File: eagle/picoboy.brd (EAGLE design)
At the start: 72 x 121.7 mm, 14 parts

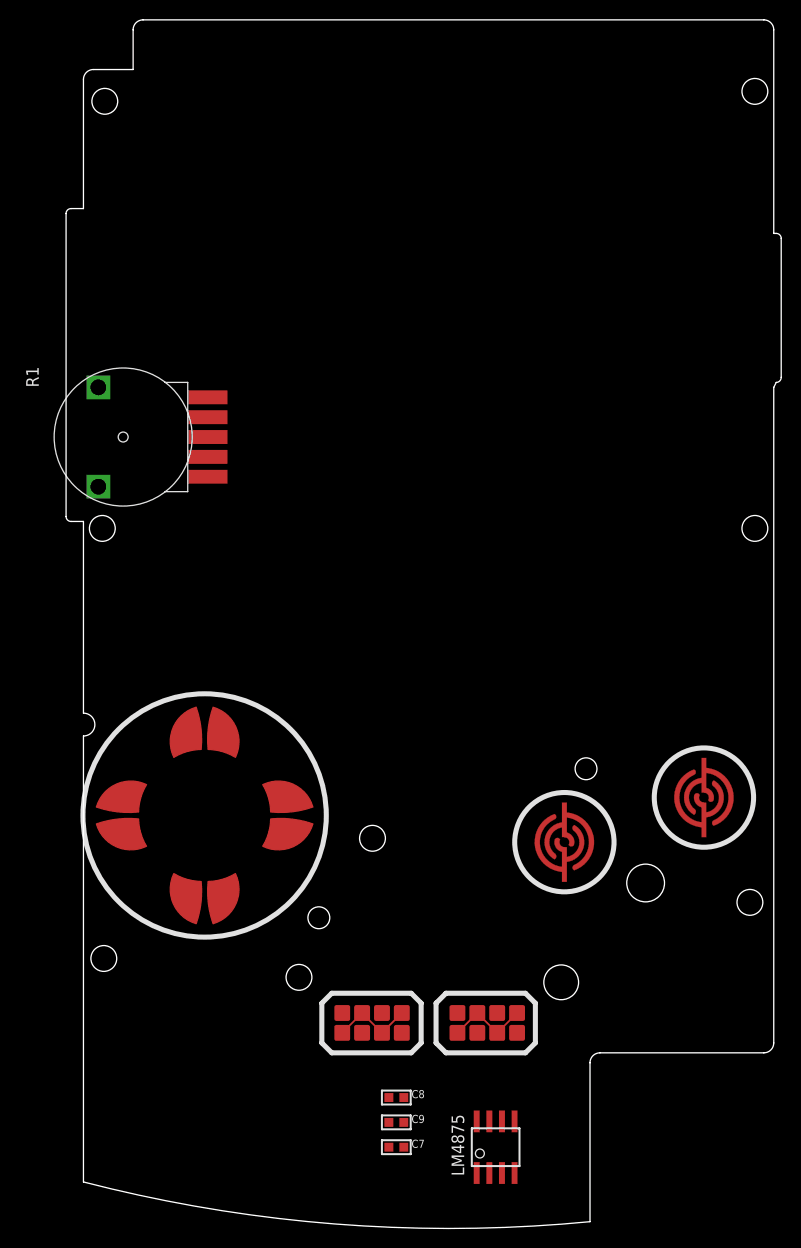
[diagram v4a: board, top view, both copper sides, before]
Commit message: Wired all audio components
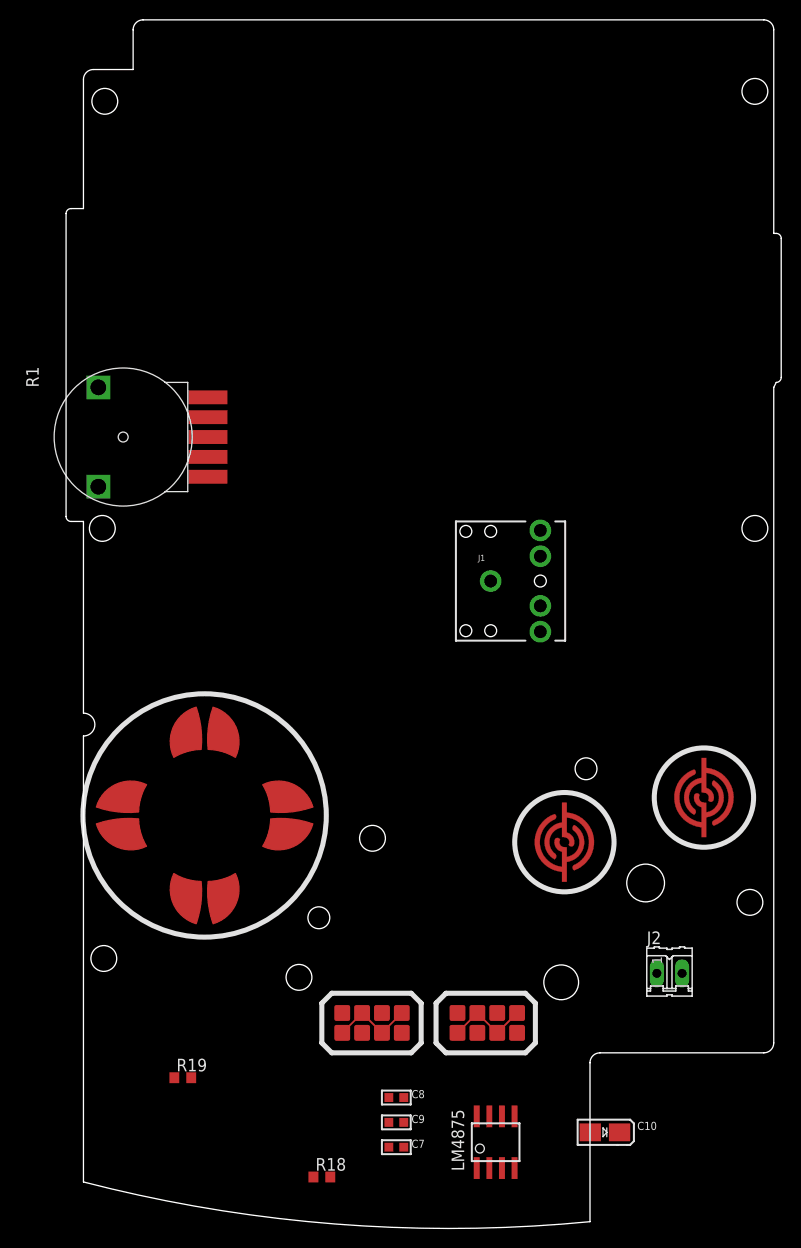
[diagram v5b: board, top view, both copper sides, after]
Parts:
- added C10: 100uF, picoboy:PICOBOY_CAPACITOR_EIA3216-18/A-W
- added J1: PICOBOY_AUDIO_JACK_3.5MM_KIT, picoboy:PICOBOY_AUDIO-JACK-KIT
- added J2: SPKR, con-amp-quick:02P
- added R18: 150 Ohms, rcl:R0603
- added R19: 100K, rcl:R0603
- moved LM4875 0.50 mm to (41.5, 4.00)
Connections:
- net N$1 renamed BYP
- net N$3 renamed VIN
- net N$4 renamed DC_VOL
- removed net N$2: C9.1, LM4875.1
- new net HPSENSE: J1.RSH, J1.TSH, LM4875.3, R19.1
- new net N$7: C10.-, J1.RING, J1.TIP, R18.2
- new net VOUT1: C10.+, J2.1, LM4875.5
- new net VOUT2: J2.2, LM4875.8
- net 3V3: now also C9.1, LM4875.1, R19.2
- net GND: now also J1.SLEEVE, R18.1
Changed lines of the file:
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@@
 <setting verticaltext="up"/>
 </settings>
-<grid distance="0.5" unitdist="mm" unit="mm" style="lines" multiple="1" display="yes" altdistance="0.125" altunitdist="mm" altunit="mm"/>
+<grid distance="0.5" unitdist="mm" unit="mm" style="lines" multiple="1" display="no" altdistance="0.125" altunitdist="mm" altunit="mm"/>
 <layers>
 <layer number="1" name="Top" color="4" fill="1" visible="yes" active="yes"/>
@@
 <element name="SELECT" library="picoboy" package="PICOBOY_CONDUCTIVE_BUTTON_THICK_STARTSELECT" value="PICOBOY_CONDUCTIVE_BUTTON_STARTSELECTCONDUCTIVE_BUTTON_THICK_STARTSELECT" x="29.055" y="16.01" smashed="yes"/>
 <element name="START" library="picoboy" package="PICOBOY_CONDUCTIVE_BUTTON_THICK_STARTSELECT" value="PICOBOY_CONDUCTIVE_BUTTON_STARTSELECTCONDUCTIVE_BUTTON_THICK_STARTSELECT" x="40.655" y="16.01" smashed="yes"/>
-<element name="LM4875" library="picoboy" package="PICOBOY_LM4875" value="PICOBOY_LM4875" x="41.5" y="3.5" smashed="yes">
-<attribute name="NAME" x="38.333" y="0.595" size="1.27" layer="25" rot="R90"/>
+<element name="LM4875" library="picoboy" package="PICOBOY_LM4875" value="PICOBOY_LM4875" x="41.5" y="4" smashed="yes">
+<attribute name="NAME" x="38.333" y="1.095" size="1.27" layer="25" rot="R90"/>
 </element>
 <element name="U$1" library="picoboy" package="PICOBOY_GBC_BOARD_OUTLINE" value="" x="0" y="0" smashed="yes"/>
@@
 <attribute name="NAME" x="-4.5" y="80" size="1.27" layer="25" rot="R90"/>
 <attribute name="VALUE" x="-2.5" y="80" size="1.27" layer="27" rot="R90"/>
+</element>
+<element name="J2" library="con-amp-quick" library_urn="urn:adsk.eagle:library:125" package="02P" package3d_urn="urn:adsk.eagle:package:5956/1" value="SPKR" x="59" y="21" smashed="yes">
+<attribute name="MF" value="" x="59" y="21" size="1.778" layer="27" display="off"/>
+<attribute name="MPN" value="" x="59" y="21" size="1.778" layer="27" display="off"/>
+<attribute name="NAME" x="56.714" y="23.9464" size="1.27" layer="25" ratio="10"/>
+<attribute name="OC_FARNELL" value="unknown" x="59" y="21" size="1.778" layer="27" display="off"/>
+<attribute name="OC_NEWARK" value="unknown" x="59" y="21" size="1.778" layer="27" display="off"/>
+<attribute name="POPULARITY" value="33" x="59" y="21" size="1.778" layer="27" display="off"/>
+<attribute name="VALUE" x="56.714" y="17.1646" size="1.27" layer="27" ratio="10"/>
+</element>
+<element name="J1" library="picoboy" package="PICOBOY_AUDIO-JACK-KIT" value="PICOBOY_AUDIO_JACK_3.5MM_KIT" x="41" y="60.5" smashed="yes">
+<attribute name="NAME" x="39.73" y="62.532" size="0.6096" layer="25" font="vector" ratio="20"/>
+<attribute name="PROD_ID" value="CONN-10353" x="41" y="60.5" size="1.778" layer="27" display="off"/>
+<attribute name="SF_ID" value="PRT-08032" x="41" y="60.5" size="1.778" layer="27" display="off"/>
+<attribute name="VALUE" x="39.73" y="57.833" size="0.6096" layer="27" font="vector" ratio="20"/>
+</element>
+<element name="R19" library="rcl" library_urn="urn:adsk.eagle:library:334" package="R0603" package3d_urn="urn:adsk.eagle:package:23555/3" value="100K" x="10" y="10.5" smashed="yes">
+<attribute name="NAME" x="9.365" y="11.135" size="1.27" layer="25"/>
+<attribute name="POPULARITY" value="77" x="10" y="10.5" size="1.778" layer="27" display="off"/>
+<attribute name="SPICEPREFIX" value="R" x="10" y="10.5" size="1.778" layer="27" display="off"/>
+<attribute name="VALUE" x="9.365" y="8.595" size="1.27" layer="27"/>
+</element>
+<element name="R18" library="rcl" library_urn="urn:adsk.eagle:library:334" package="R0603" package3d_urn="urn:adsk.eagle:package:23555/3" value="150 Ohms" x="24" y="0.5" smashed="yes">
+<attribute name="NAME" x="23.365" y="1.135" size="1.27" layer="25"/>
+<attribute name="POPULARITY" value="77" x="24" y="0.5" size="1.778" layer="27" display="off"/>
+<attribute name="SPICEPREFIX" value="R" x="24" y="0.5" size="1.778" layer="27" display="off"/>
+<attribute name="VALUE" x="23.365" y="-1.405" size="1.27" layer="27"/>
+</element>
+<element name="C10" library="picoboy" package="PICOBOY_CAPACITOR_EIA3216-18/A-W" value="100uF" x="52.5" y="5" smashed="yes">
+<attribute name="NAME" x="55.757" y="5.238" size="0.8128" layer="25" ratio="18"/>
+<attribute name="VALUE" x="55.757" y="4.326" size="0.4064" layer="27" ratio="10"/>
 </element>
 </elements>
@@
 <contactref element="C9" pad="2"/>
 <contactref element="R1" pad="1"/>
+<contactref element="R18" pad="1"/>
+<contactref element="J1" pad="SLEEVE"/>
 <wire x1="32.25" y1="8.5" x2="12.5" y2="71" width="0" layer="19" extent="1-1"/>
 <wire x1="32.25" y1="6" x2="32.25" y2="8.5" width="0" layer="19" extent="1-1"/>
-<wire x1="42.135" y1="6.1" x2="32.25" y2="6" width="0" layer="19" extent="1-1"/>
-</signal>
-<signal name="N$1">
+<wire x1="42.135" y1="6.6" x2="32.25" y2="6" width="0" layer="19" extent="1-1"/>
+<wire x1="41" y1="60.5" x2="32.25" y2="6" width="0" layer="19" extent="1-1"/>
+<wire x1="23.15" y1="0.5" x2="41" y2="60.5" width="0" layer="19" extent="1-1"/>
+</signal>
+<signal name="BYP">
 <contactref element="LM4875" pad="7"/>
 <contactref element="C8" pad="1"/>
-<wire x1="30.75" y1="8.5" x2="40.865" y2="6.1" width="0" layer="19" extent="1-1"/>
-</signal>
-<signal name="N$2">
+<wire x1="30.75" y1="8.5" x2="40.865" y2="6.6" width="0" layer="19" extent="1-1"/>
+</signal>
+<signal name="VIN">
+<contactref element="LM4875" pad="2"/>
+<contactref element="C7" pad="2"/>
+<wire x1="32.25" y1="3.5" x2="40.865" y2="1.4" width="0" layer="19" extent="1-1"/>
+</signal>
+<signal name="DC_VOL">
+<contactref element="R1" pad="3"/>
+<contactref element="LM4875" pad="4"/>
+<wire x1="43.405" y1="1.4" x2="12.5" y2="75" width="0" layer="19" extent="1-1"/>
+</signal>
+<signal name="3V3">
+<contactref element="R1" pad="5"/>
 <contactref element="LM4875" pad="1"/>
 <contactref element="C9" pad="1"/>
-<wire x1="30.75" y1="6" x2="39.595" y2="0.9" width="0" layer="19" extent="1-1"/>
-</signal>
-<signal name="N$3">
-<contactref element="LM4875" pad="2"/>
-<contactref element="C7" pad="2"/>
-<wire x1="32.25" y1="3.5" x2="40.865" y2="0.9" width="0" layer="19" extent="1-1"/>
-</signal>
-<signal name="N$4">
-<contactref element="R1" pad="3"/>
-<contactref element="LM4875" pad="4"/>
-<wire x1="43.405" y1="0.9" x2="12.5" y2="75" width="0" layer="19" extent="1-1"/>
-</signal>
-<signal name="3V3">
-<contactref element="R1" pad="5"/>
+<contactref element="R19" pad="2"/>
+<wire x1="10.85" y1="10.5" x2="12.5" y2="79" width="0" layer="19" extent="1-1"/>
+<wire x1="30.75" y1="6" x2="10.85" y2="10.5" width="0" layer="19" extent="1-1"/>
+<wire x1="39.595" y1="1.4" x2="30.75" y2="6" width="0" layer="19" extent="1-1"/>
 </signal>
 <signal name="AUDIO">
 <contactref element="C7" pad="1"/>
+</signal>
+<signal name="VOUT1">
+<contactref element="LM4875" pad="5"/>
+<contactref element="J2" pad="1"/>
+<contactref element="C10" pad="+"/>
+<wire x1="43.405" y1="6.6" x2="57.73" y2="21" width="0" layer="19" extent="1-1"/>
+<wire x1="53.975" y1="5" x2="43.405" y2="6.6" width="0" layer="19" extent="1-1"/>
+</signal>
+<signal name="VOUT2">
+<contactref element="LM4875" pad="8"/>
+<contactref element="J2" pad="2"/>
+<wire x1="39.595" y1="6.6" x2="60.27" y2="21" width="0" layer="19" extent="1-1"/>
+</signal>
+<signal name="HPSENSE">
+<contactref element="LM4875" pad="3"/>
+<contactref element="J1" pad="RSH"/>
+<contactref element="J1" pad="TSH"/>
+<contactref element="R19" pad="1"/>
+<wire x1="46" y1="58" x2="46" y2="63" width="0" layer="19" extent="1-1"/>
+<wire x1="42.135" y1="1.4" x2="46" y2="58" width="0" layer="19" extent="1-1"/>
+<wire x1="9.15" y1="10.5" x2="42.135" y2="1.4" width="0" layer="19" extent="1-1"/>
+</signal>
+<signal name="N$7">
+<contactref element="J1" pad="TIP"/>
+<contactref element="C10" pad="-"/>
+<contactref element="J1" pad="RING"/>
+<contactref element="R18" pad="2"/>
+<wire x1="24.85" y1="0.5" x2="51.025" y2="5" width="0" layer="19" extent="1-1"/>
+<wire x1="46" y1="55.4" x2="24.85" y2="0.5" width="0" layer="19" extent="1-1"/>
+<wire x1="46" y1="65.6" x2="46" y2="55.4" width="0" layer="19" extent="1-1"/>
 </signal>
 </signals>
@@
 </board>
 </drawing>
+<compatibility>
+<note version="8.2" severity="warning">
+Since Version 8.2, EAGLE supports online libraries. The ids
+of those online libraries will not be understood (or retained)
+with this version.
+</note>
+<note version="8.3" severity="warning">
+Since Version 8.3, EAGLE supports URNs for individual library
+assets (packages, symbols, and devices). The URNs of those assets
+will not be understood (or retained) with this version.
+</note>
+<note version="8.3" severity="warning">
+Since Version 8.3, EAGLE supports the association of 3D packages
+with devices in libraries, schematics, and board files. Those 3D
+packages will not be understood (or retained) with this version.
+</note>
+</compatibility>
 </eagle>
